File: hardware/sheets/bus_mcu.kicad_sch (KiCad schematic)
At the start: 64 parts, among them M1 Core2350B (0MB PSRAM), U10 74HC161, U11 74HC161, U12 74HCT165, U13 74LVC245A, U14 74HCT244, U15 74HCT244, U16 74HCT244, U17 74HCT04, U18 74HC08, U19 74HCT165, U2 74LVC245A, U3 74LVC245A, U4 74LVC245A, U5 74LVC245A, U6 74LVC245A, U7 74HC161, U8 74HC161, U9 74HC161

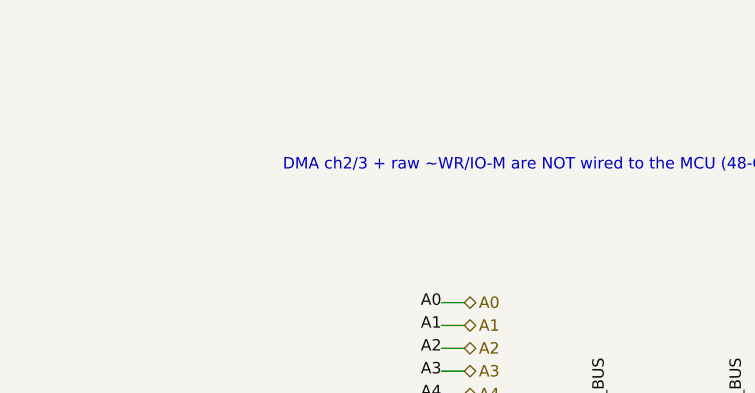
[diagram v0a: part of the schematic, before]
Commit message: ERC power cleanup: single flag owner, flags on series-fed rails
Full-build ERC is now just the 6 expected IRQ9-13/15 label_dangling.

- Root's duplicate PWR_FLAGs removed from build.py: power.py #FLG1-3
  own +5V/+3V3/GND; the pair made flag-vs-flag pin_to_pin errors.
- PWR_FLAGs added on the local rails ERC can't see through a series
  part: VBUS_MCU / VBUS_VID (Schottky diode-OR), VBUS_KBD / HDMI_5V
  (polyfuse), CH224_VDD (1k per WCH ref), AVDD_PGUS / AGND_PGUS
  (ferrite beads).

Net membership verified unchanged: 821 nets, node-identical to HEAD.

Co-Authored-By: Claude Fable 5 <noreply@anthropic.com>
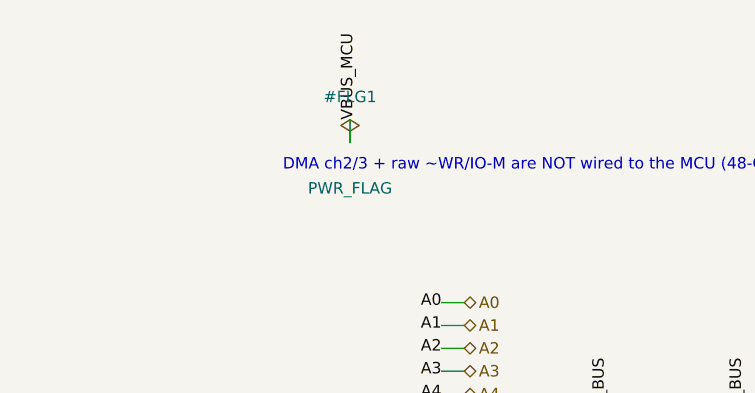
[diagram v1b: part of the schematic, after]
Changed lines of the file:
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@@
 	(wire
 		(pts
+			(xy 12.7 12.7)
+			(xy 12.7 10.16)
+		)
+		(stroke
+			(width 0)
+			(type default)
+		)
+	)
+	(label "VBUS_MCU"
+		(at 12.7 10.16 90)
+		(effects
+			(font
+				(size 1.27 1.27)
+			)
+		)
+	)
+	(wire
+		(pts
 			(xy 200.66 59.69)
 			(xy 200.66 57.15)
@@
 					(unit 1)
 				)
+			)
+		)
+	)
+	(symbol
+		(lib_id "power:PWR_FLAG")
+		(at 12.7 12.7 0)
+		(unit 1)
+		(exclude_from_sim no)
+		(in_bom yes)
+		(on_board yes)
+		(dnp no)
+		(fields_autoplaced yes)
+		(property "Reference" "#FLG1"
+			(at 12.7 7.62 0)
+			(effects
+				(font
+					(size 1.27 1.27)
+				)
+			)
+		)
+		(property "Value" "PWR_FLAG"
+			(at 12.7 17.78 0)
+			(effects
+				(font
+					(size 1.27 1.27)
+				)
+			)
+		)
+		(property "Footprint" ""
+			(at 12.7 12.7 0)
+			(effects
+				(font
+					(size 1.27 1.27)
+				)
+				(hide yes)
+			)
+		)
+		(pin "1"
+		)
+		(instances
+			(project "mini-xt"
+				(path "/26736c46-8b40-5460-874f-03596d17270c/1e41a345-3dfb-5180-bb4f-8215c959e5d6"
+					(reference "#FLG201")
+					(unit 1)
+				)

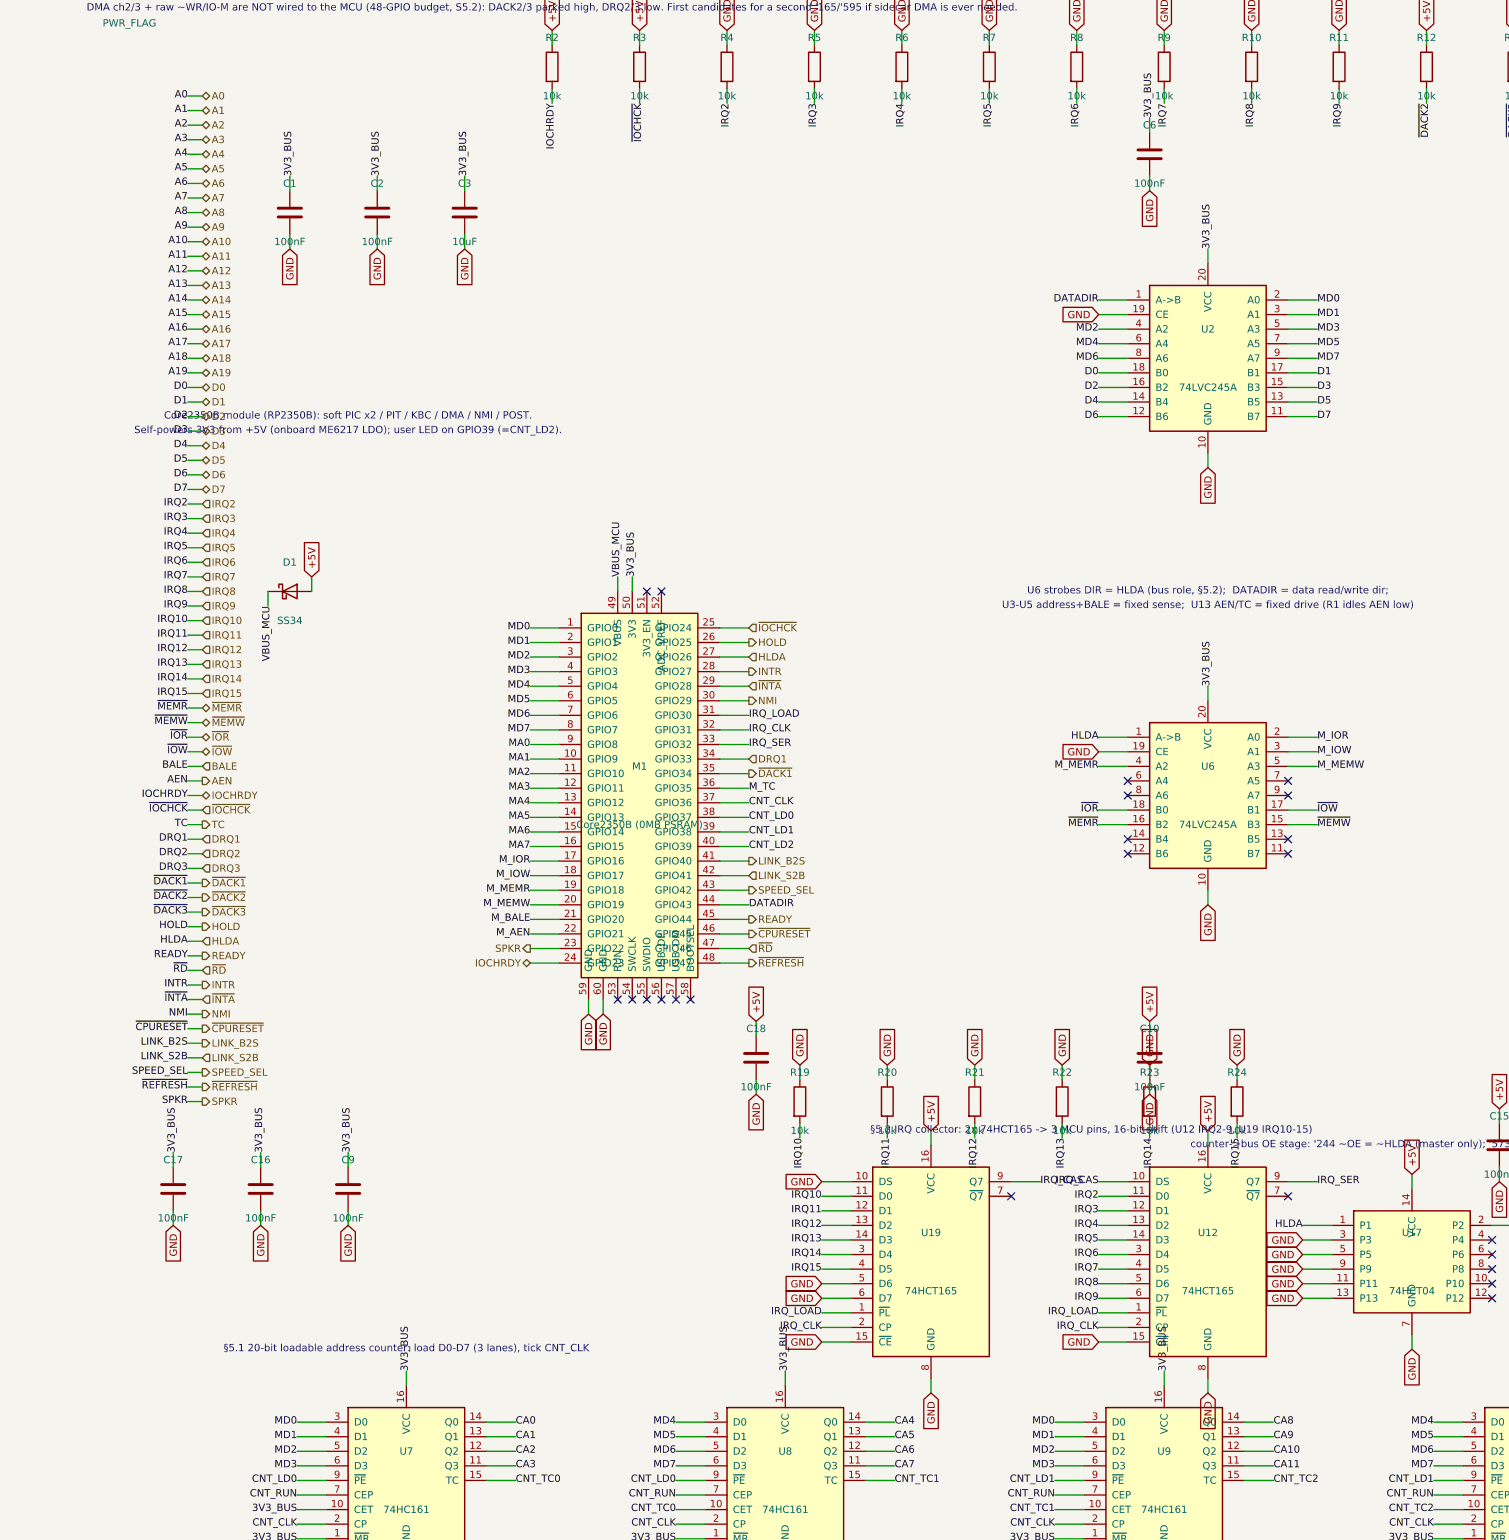
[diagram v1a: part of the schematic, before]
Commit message: IRQ rework: single-'165 collector, hardwired COM/LPT IRQs
- IRQ collector shrunk to one 74HCT165: D0-D6 = IRQ2-8, D7 = IRQ14
  (replacing the source-less IRQ9). U19 + pull-downs R19-R24 + C18
  deleted; IRQ9-13/15 dropped everywhere (nothing on the board or the
  8-bit header can drive them). Firmware shifts 8 bits, Q7-first.
- COM/LPT IRQ straps deleted, hardwired to the PC conventions:
  COM1=IRQ4, COM2=IRQ3 (COM_IRQ per-instance netmap remap -- first use
  of the INSTANCES netmap), LPT=IRQ7 (U13 '125 drives the net
  directly). The enable jumpers (COM JP3, LPT JP2) free an IRQ by
  disabling the port; the tri-state drivers go silent with it.
- Storage JP3 (IRQ14/IRQ5) kept: both positions are real conventions
  (AT vs XT), not conflict avoidance. Its IRQ5 warning now points at
  the PicoGUS jumper block, the only remaining IRQ5 contention.
- Design doc: fix stale claim that IRQ8 rides a reclaimed header pin
  (that pin is a ground return; IRQ8 is motherboard-internal).

Full-build ERC: 0 violations.

Co-Authored-By: Claude Fable 5 <noreply@anthropic.com>
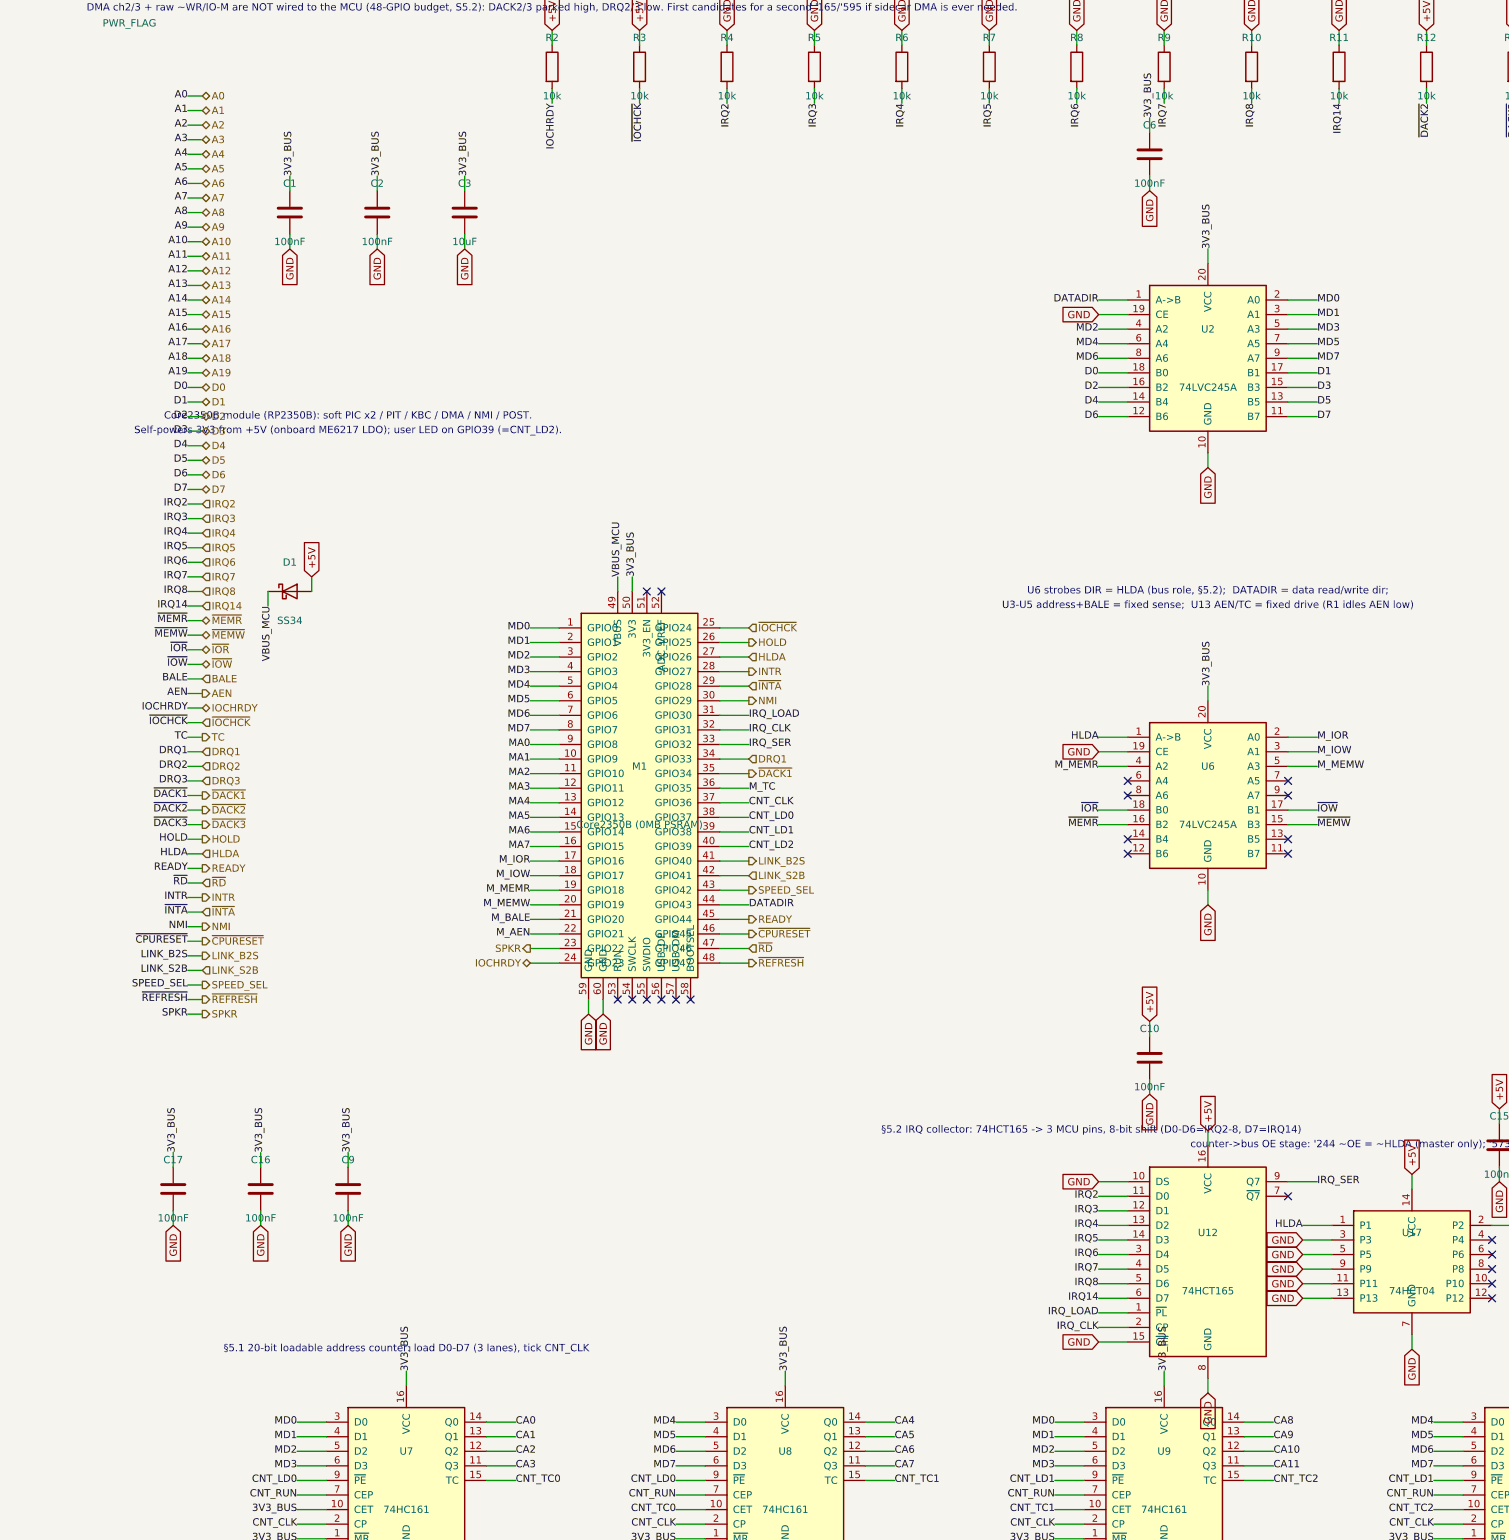
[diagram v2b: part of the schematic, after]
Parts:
- removed C18: 100nF, symbol Device:C
- removed R12, R13, R14, R15, R16, R17, R18, R20, R21, R22, R23, R24, R25, R26, R27, R28: 10k, symbol Device:R
- removed U19: 74HCT165, symbol mini-xt:74HCT165
- removed U5: 74LVC245A, symbol mini-xt:74LVC245A
- added R10, R11, R2, R3, R4, R5, R6, R7, R8, R9: 10k, symbol Device:R
- added U3: 74LVC245A, symbol mini-xt:74LVC245A
- renumbered R2 to R12, R3 to R13, R4 to R14, R5 to R15, R6 to R16, R7 to R17, R8 to R18, R9 to R25, R10 to R26, R11 to R27, R19 to R28, U3 to U5
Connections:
- net IRQ10 is gone; now on net DRQ1: R28.2
- net IRQ_CAS is gone; now on net GND: U12.10 (DS)
- net +5V: now also R2.1, R3.1
- net A0: now also U3.18 (B0); no longer U5.18 (B0)
- net A1: now also U3.17 (B1); no longer U5.17 (B1)
- net A16: now also U5.18 (B0)
- net A17: now also U5.17 (B1)
- net A18: now also U5.16 (B2)
- net A19: now also U5.15 (B3)
- net A2: now also U3.16 (B2); no longer U5.16 (B2)
- net A3: now also U3.15 (B3); no longer U5.15 (B3)
- net A4: now also U3.14 (B4); no longer U5.14 (B4)
- net A5: now also U3.13 (B5); no longer U5.13 (B5)
- net A6: now also U3.12 (B6); no longer U5.12 (B6)
- net A7: now also U3.11 (B7); no longer U5.11 (B7)
- net BALE: now also U5.14 (B4)
- net DATADIR: now also R16.2
- net DRQ2: now also R14.2
- net DRQ3: now also R15.2
- net GND: now also R10.1, R11.1, R4.1, R5.1, R6.1, R7.1, R8.1, R9.1, U3.1 (A->B), U3.10 (GND), U3.19 (CE), U3.20 (VCC)
- net HLDA: now also R18.2
- net IOCHRDY: now also R2.2; no longer R12.2
- net IRQ14: now also U12.6 (D7), R11.2
- net IRQ2: now also R4.2; no longer R14.2
- net IRQ3: now also R5.2; no longer R15.2
- net IRQ4: now also R6.2; no longer R16.2
- net IRQ5: now also R7.2; no longer R17.2
- net IRQ6: now also R8.2; no longer R18.2
- net IRQ7: now also R9.2; no longer R25.2
- net IRQ8: now also R10.2; no longer R26.2
- net MA0: now also U3.2 (A0); no longer U5.2 (A0)
- net MA1: now also U3.3 (A1); no longer U5.3 (A1)
- net MA16: now also U5.2 (A0)
- net MA17: now also U5.3 (A1)
- net MA18: now also U5.4 (A2)
- net MA19: now also U5.5 (A3)
- net MA2: now also U3.4 (A2); no longer U5.4 (A2)
- net MA3: now also U3.5 (A3); no longer U5.5 (A3)
- net MA4: now also U3.6 (A4); no longer U5.6 (A4)
- net MA5: now also U3.7 (A5); no longer U5.7 (A5)
- net MA6: now also U3.8 (A6); no longer U5.8 (A6)
- net MA7: now also U3.9 (A7); no longer U5.9 (A7)
- net M_BALE: now also U5.6 (A4)
- net M_TC: now also R17.2
- net ~{CPURESET}: now also R25.2
- net ~{DACK1}: now also R26.2
- net ~{DACK2}: now also R12.2
- net ~{DACK3}: now also R13.2
- net ~{IOCHCK}: now also R3.2; no longer R13.2
- net ~{REFRESH}: now also R27.2
- removed net IRQ9: R27.2, U12.6 (D7)
- no-connect marks 48 -> 47
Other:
- note added: "§5.2 IRQ collector: 74HCT165 -> 3 MCU pins, 8-bit shift (D0-D6=IRQ2-8, D7=IRQ14)"
- note removed: "§5.2 IRQ collector: 2x 74HCT165 -> 3 MCU pins, 16-bit shift (U12 IRQ2-9, U19 IRQ10-15)"
- moved on the sheet: R12, R13, R14, R15, R16, R17, R18, R25, R26, R27, R28, U5
